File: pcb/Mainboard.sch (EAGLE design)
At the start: 13 parts

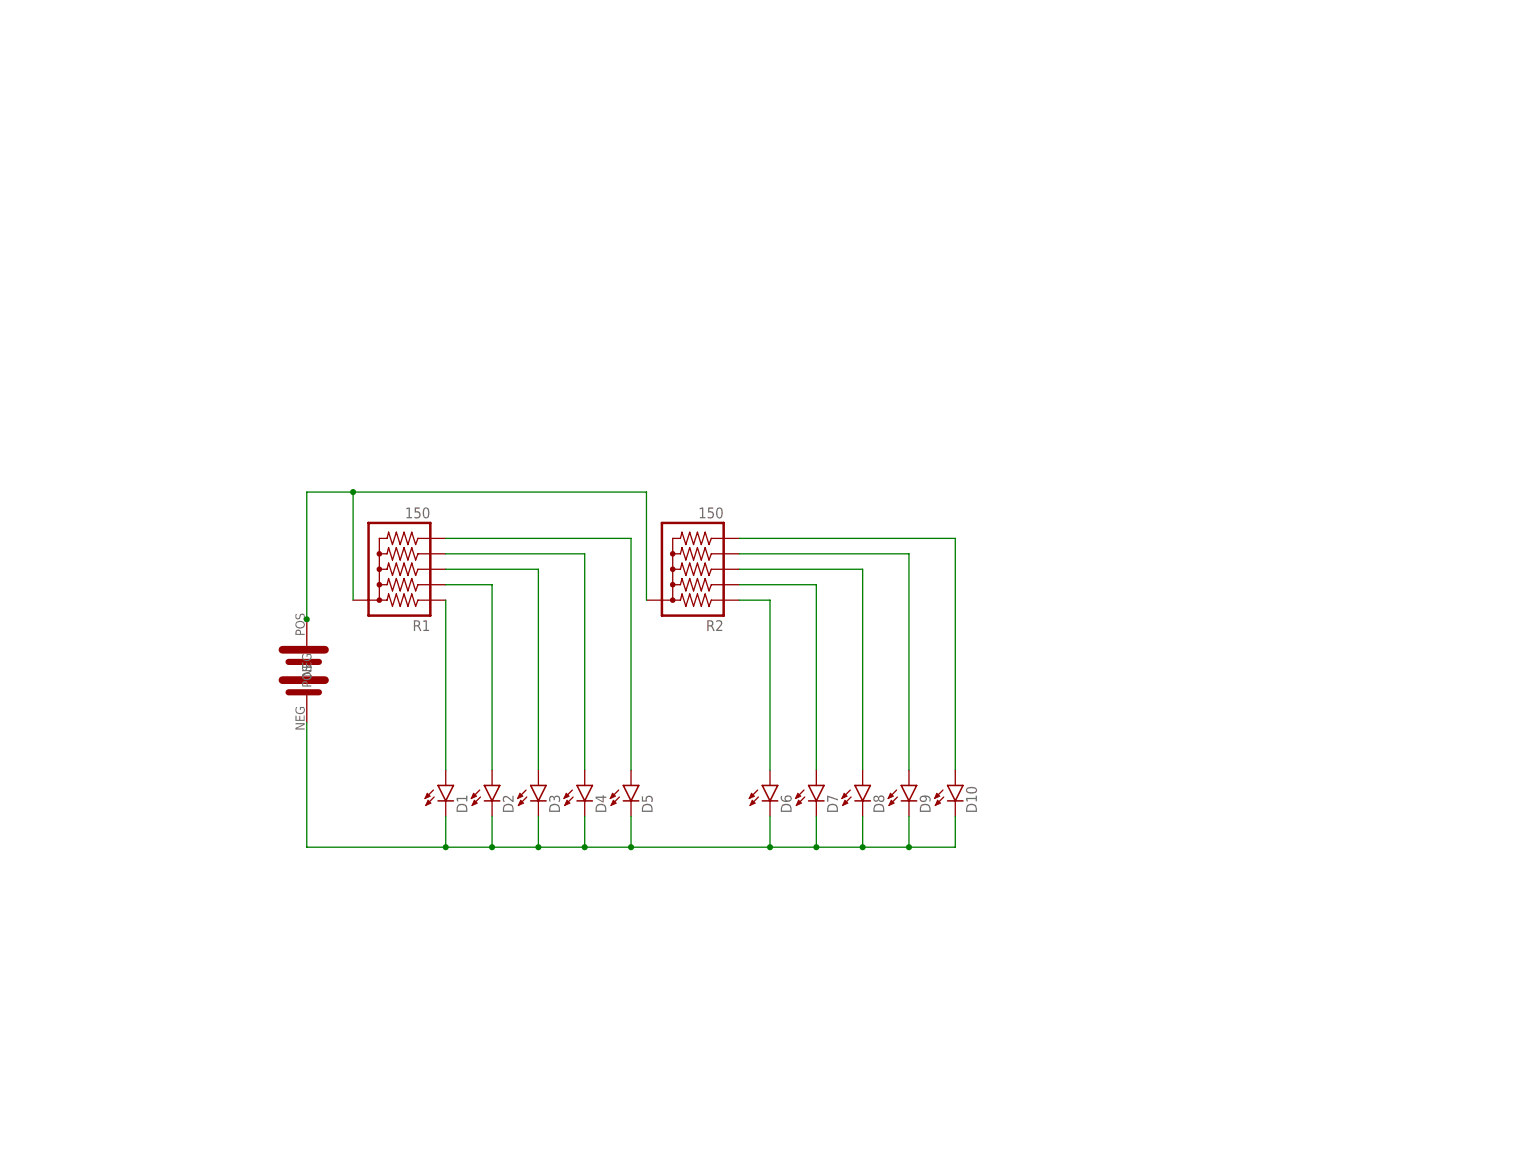
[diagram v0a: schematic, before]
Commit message: Started SMD redesign.
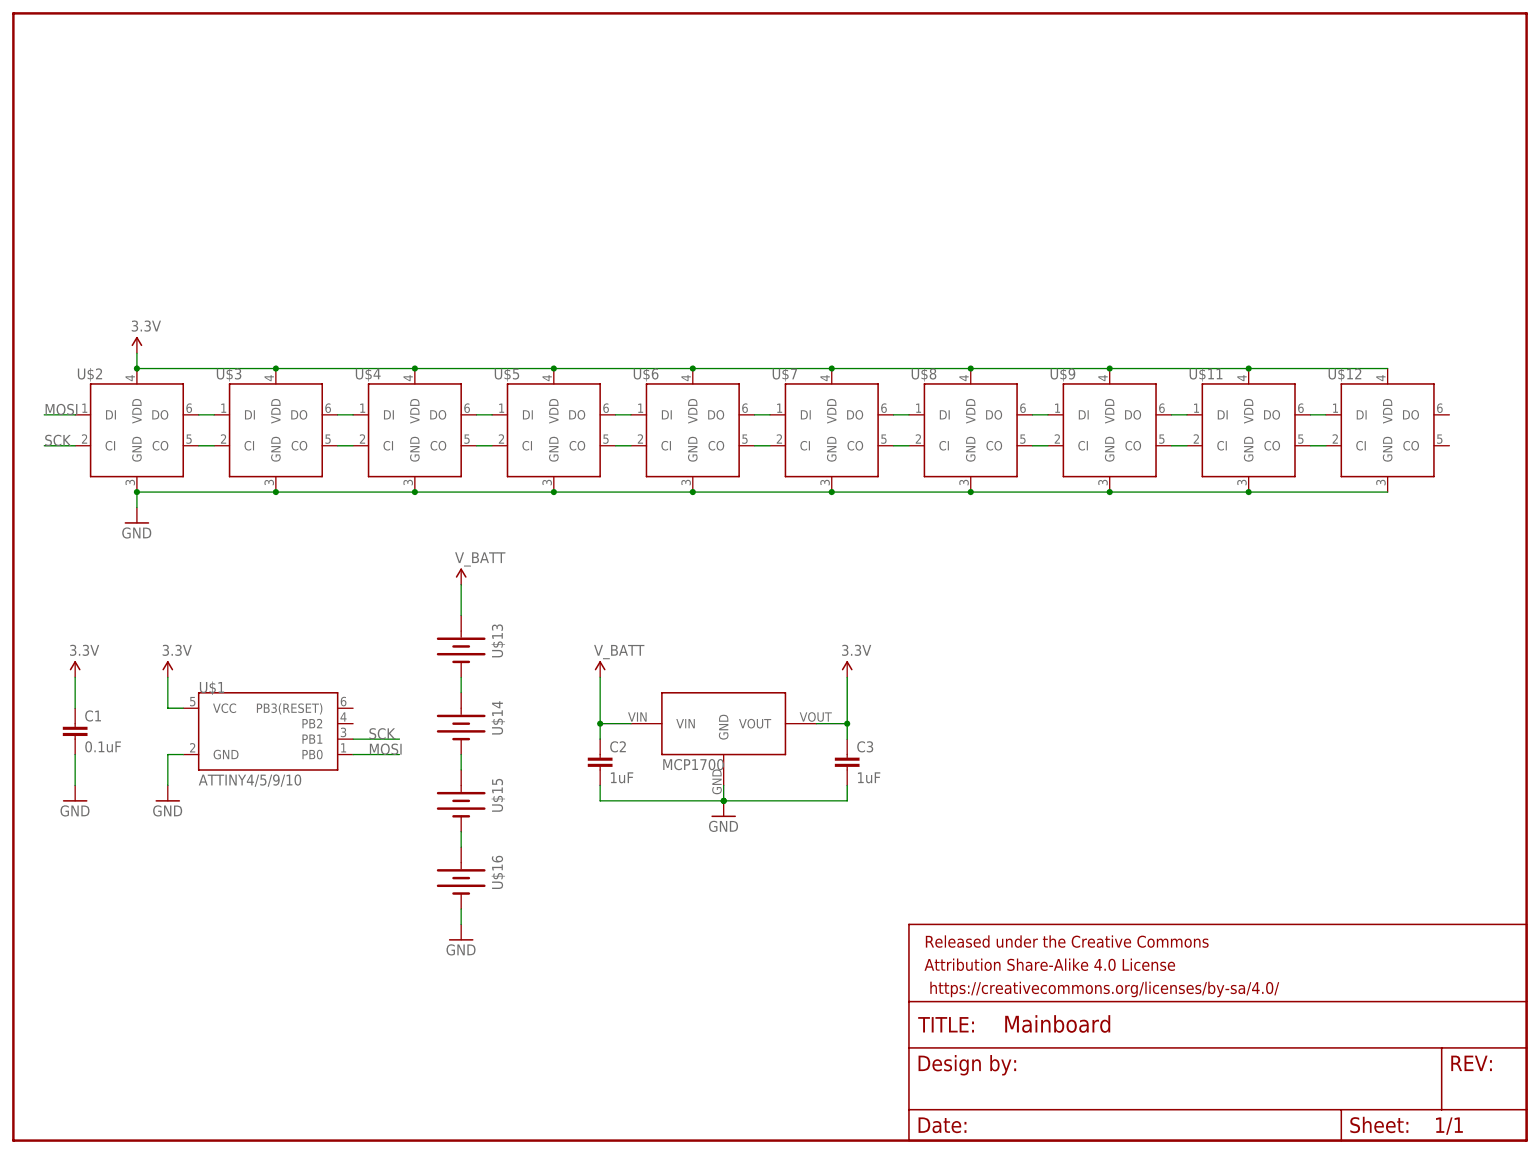
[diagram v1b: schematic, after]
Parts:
- removed D1, D10, D2, D3, D4, D5, D6, D7, D8, D9: (no value), SparkFun-LED:LED5MM
- removed R1, R2: 150, SparkFun-Resistors:RPACK-BUSSED-5-SIP-PTH-5
- added C1: 0.1uF, SparkFun-Passives:CAP0402-CAP
- added C2, C3: 1uF, SparkFun-Passives:CAP0402-CAP
- added FRAME1: FRAME-LETTER, SparkFun-Aesthetics:FRAME-LETTER
- added U$11, U$12, U$2, U$3, U$4, U$5, U$6, U$7, U$8, U$9: APA102C, OpenSourceArt_Eagle_Library:APA102C
- added U$13, U$14, U$15, U$16: AAAA-BATTERYS, OpenSourceArt_Eagle_Library:AAAA-BATTERYS
- added U$17: MCP1700, OpenSourceArt_Eagle_Library:MCP1700
- U$1: value KEYSTONE-TH-CR2450 -> ATTINY4/5/9/10; device winn:KEYSTONE-TH-CR2450 -> OpenSourceArt_Eagle_Library:ATTINY4/5/9/10
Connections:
- removed net N$7: D6.A, R2.2
- removed net VCC: R1.1, R2.1, U$1.POS
- new net 3.3V: C1.1, C3.1, U$1.VCC, U$11.VDD, U$12.VDD, U$17.VOUT, U$2.VDD, U$3.VDD, U$4.VDD, U$5.VDD, U$6.VDD, U$7.VDD, U$8.VDD, U$9.VDD
- new net MOSI: U$1.PB0, U$2.DI
- new net N$11: U$4.DO, U$5.DI
- new net N$12: U$3.DO, U$4.DI
- new net N$13: U$7.DO, U$8.DI
- new net N$14: U$7.CO, U$8.CI
- new net N$15: U$8.DO, U$9.DI
- new net N$16: U$8.CO, U$9.CI
- new net N$17: U$11.DI, U$9.DO
- new net N$18: U$11.CI, U$9.CO
- new net N$19: U$11.DO, U$12.DI
- new net N$20: U$11.CO, U$12.CI
- new net N$23: U$14.-, U$15.+
- new net N$24: U$15.-, U$16.+
- new net SCK: U$1.PB1, U$2.CI
- new net V_BATT: C2.1, U$13.+, U$17.VIN
- net GND: now also C1.2, C2.2, C3.2, U$1.GND, U$11.GND, U$12.GND, U$16.-, U$17.GND, U$2.GND, U$3.GND, U$4.GND, U$5.GND, U$6.GND, U$7.GND, U$8.GND, U$9.GND; no longer D1.C, D10.C, D2.C, D3.C, D4.C, D5.C, D6.C, D7.C, D8.C, D9.C, U$1.NEG
- net N$1: now also U$2.DO, U$3.DI; no longer D4.A, R1.5
- net N$10: now also U$5.DO, U$6.DI; no longer D10.A, R2.6
- net N$2: now also U$2.CO, U$3.CI; no longer D1.A, R1.2
- net N$3: now also U$3.CO, U$4.CI; no longer D2.A, R1.3
- net N$4: now also U$4.CO, U$5.CI; no longer D3.A, R1.4
- net N$5: now also U$5.CO, U$6.CI; no longer D5.A, R1.6
- net N$6: now also U$13.-, U$14.+; no longer D7.A, R2.3
- net N$8: now also U$6.CO, U$7.CI; no longer D9.A, R2.5
- net N$9: now also U$6.DO, U$7.DI; no longer D8.A, R2.4
